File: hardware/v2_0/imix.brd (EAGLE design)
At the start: 87 x 102.5 mm, 156 parts, among them J2_3_5_AND_6 ARDUINO_R3NO_HOLES, SW1 TAC_SWITCHSMD, SW2 TAC_SWITCHSMD, U1 BQ2423X, U10 ISL29035, U11 FX0S8700CQ, U12 296-12686-1-ND, U13 SIP32401A, U14 SIP32401A, U15 SIP32401A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

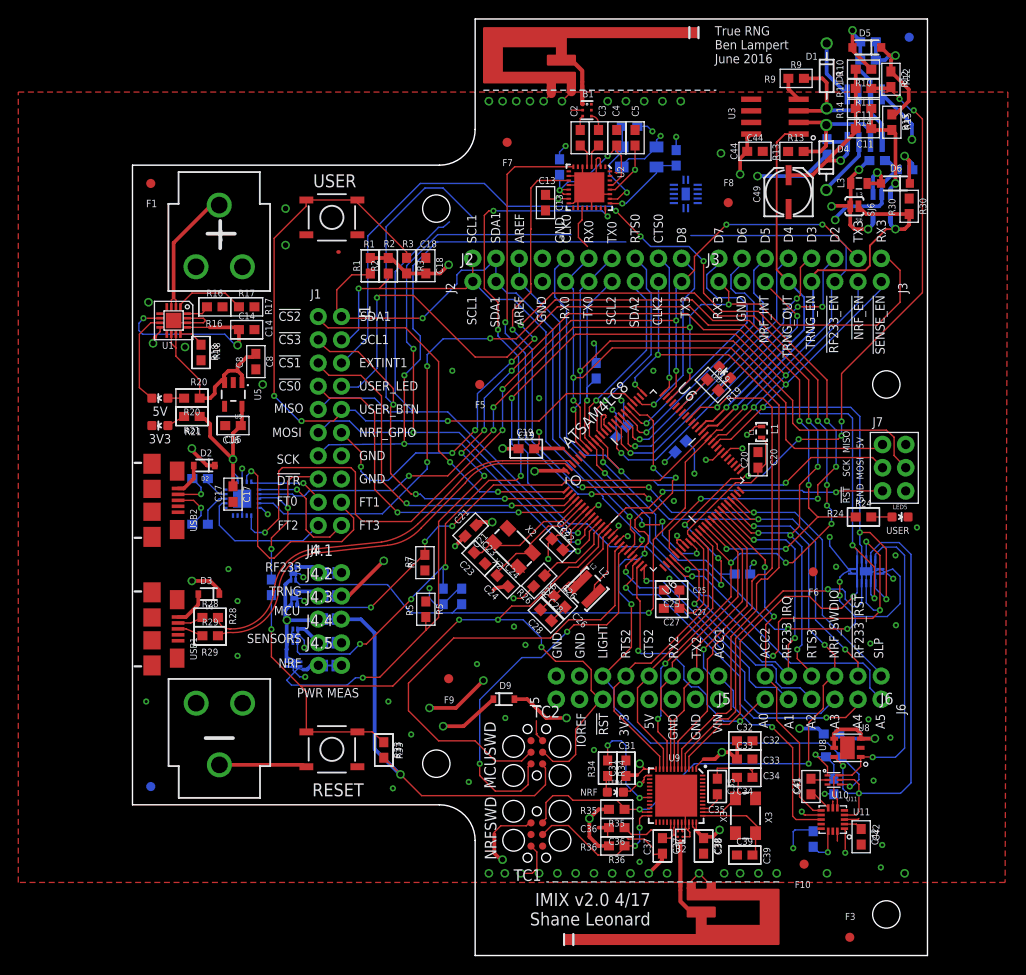
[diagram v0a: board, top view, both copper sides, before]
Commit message: One analog switch and all power switches routed
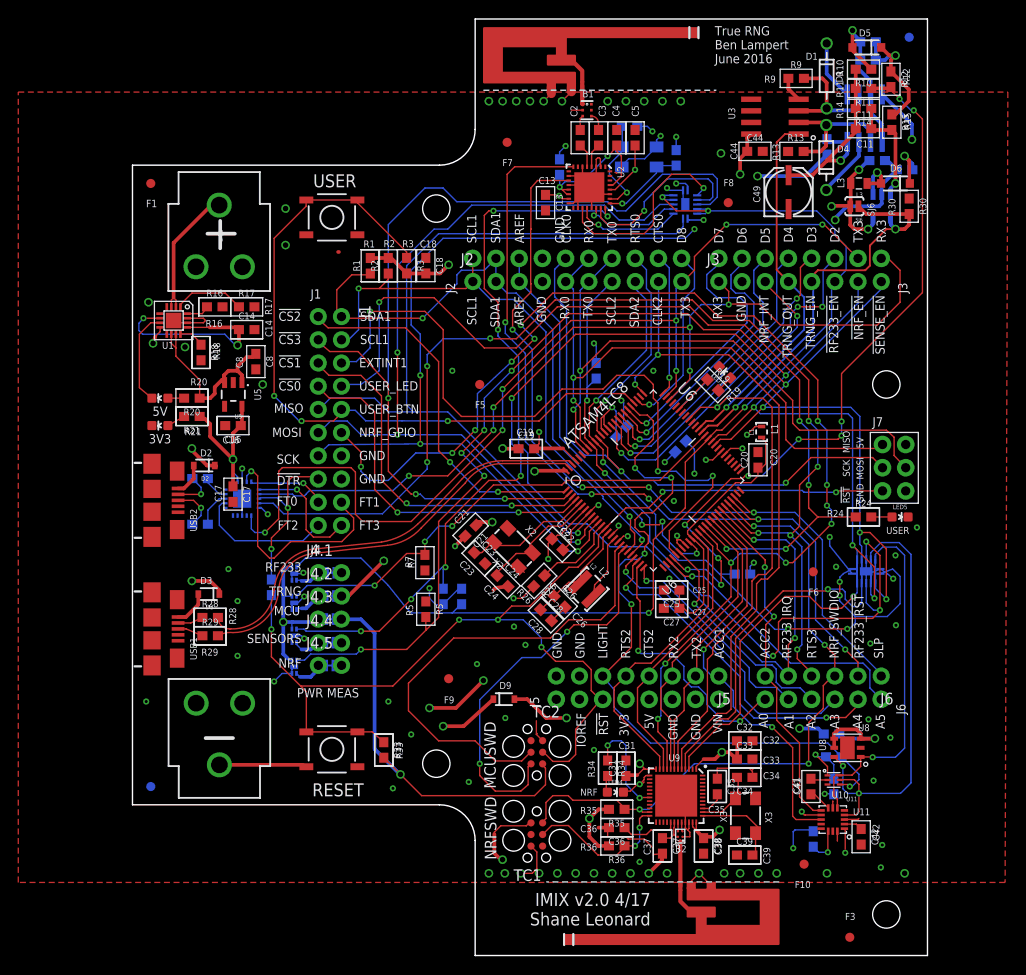
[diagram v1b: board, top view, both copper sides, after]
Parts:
- moved U17 1.15 mm to (60.5, 65.7), turned to 90 degrees
- moved U16 0.50 mm to (17.7, 22.1)
- moved U14 0.32 mm to (17.7, 15.1), turned to 180 degrees
- moved U13 0.10 mm to (17.7, 18.5)
- moved U15 0.10 mm to (17.7, 25.3)
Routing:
- net EXTINT1: track 113.7 -> 77.5 mm, vias 7 -> 3
- net SPI_NCS3: track 73.3 -> 104.8 mm
- net MISO: track 61.9 -> 86.8 mm
- net RF233_CS: track 0.00 -> 19.8 mm, vias 0 -> 1
- net VCC_MCU_3V3: track 112.9 -> 130.9 mm, vias 14 -> 15
- net RF233_SCK: track 4.82 -> 21.8 mm, vias 0 -> 1
- net SCK: track 82.9 -> 97.9 mm, vias 3 -> 5
- net MOSI: track 75.7 -> 90.5 mm
- net RF233_MISO: track 0.00 -> 11.7 mm, vias 0 -> 1
- net RF233_MOSI: track 0.00 -> 10.7 mm, vias 0 -> 1
- net RF233_PWR_EN: track 110.0 -> 120.3 mm, vias 2 -> 4
- net NRF_PWR_EN: track 158.2 -> 152.1 mm
- net SENSE_PWR_EN: track 153.9 -> 150.5 mm
- net VCC_3V3: track 52.4 -> 49.3 mm
- net LIGHT_!INT: track 77.2 -> 79.4 mm
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
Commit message: All elements routed, DRC passes
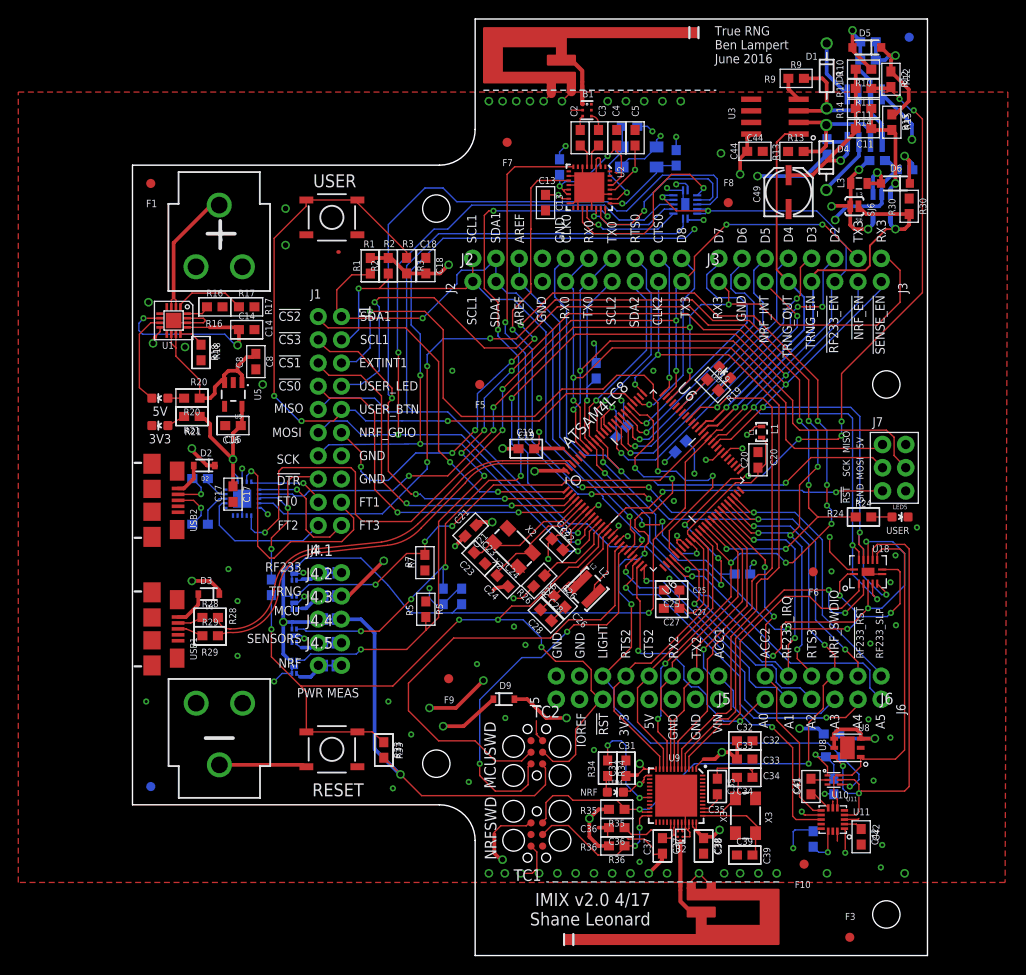
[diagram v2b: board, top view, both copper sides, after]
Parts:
- moved U18 0.21 mm to (80.5, 25.5), flipped to the top, turned to 0 degrees
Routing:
- net SENSE_PWR_EN: track 150.5 -> 144.1 mm
- net NRF_PWR_EN: track 152.1 -> 147.4 mm
- net NRF_TWI_SDA: track 36.6 -> 34.0 mm, vias 1 -> 0
- net SENSE_TWI_SCL: track 52.8 -> 50.4 mm
- net SENSE_TWI_SDA: track 41.4 -> 38.9 mm, vias 1 -> 0
- net GND: track 220.4 -> 218.5 mm
- net NRF_TWI_SCL: track 39.3 -> 37.5 mm, vias 1 -> 2
- net USER_LED: track 100.8 -> 101.5 mm
- net N$2: track 17.3 -> 16.7 mm
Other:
- board text removed: "SLP"

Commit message: v2.0 quick batch
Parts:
- moved SJ2 4.32 mm to (25.9, 15.3), turned to 0 degrees
- moved SJ1 4.30 mm to (25.9, 17.8), turned to 180 degrees
- moved SJ4 4.28 mm to (25.9, 20.2), turned to 0 degrees
- moved SJ7 4.20 mm to (25.9, 22.6), turned to 0 degrees
- moved SJ3 4.15 mm to (25.8, 25.6), turned to 0 degrees
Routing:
- net N$8: track 3.65 -> 11.0 mm
- net N$18: track 4.06 -> 11.3 mm
- net N$33: track 3.53 -> 10.5 mm
- net VCC_3V3: track 49.3 -> 56.1 mm
- net N$32: track 3.80 -> 10.5 mm
- net VCC_MCU_3V3: track 131.1 -> 135.5 mm
- net RF233_PWR_EN: track 120.3 -> 123.6 mm
- net VCC_TRNG_3V3: track 115.2 -> 117.0 mm
- net VCC_RF233_3V3: track 9.74 -> 11.5 mm
- net VCC_SENSE_3V3: track 82.6 -> 84.4 mm
- net VCC_NRF_3V3: track 52.1 -> 53.9 mm
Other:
- board text added: "0.063""
- board text added: "0.5 oz"
- board text added: "1 oz"
- board text added: "Cut to measure PWR"
- board text added: "IMIX v2.0 7/17 Shane Leonard"
- board text added: "IMIX v2.0 June 2017 Shane Leonard"
- board text added: "Inner Copper Weight"
- board text added: "M"
- board text added: "N"
- board text added: "Outer Copper Weight"
- board text added: "PCB Thickness"
- board text added: "R"
- board text added: "Red"
- board text added: "S"
- board text added: "Solder Mask Color"
- board text added: "T"
- board text removed: "Cut to measure power"
- board text removed: "IMIX v2.0 4/17 Shane Leonard"
- board text removed: "IMIX v2.0 Apr 2017 Shane Leonard"
